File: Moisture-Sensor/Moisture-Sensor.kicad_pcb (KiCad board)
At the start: 2 copper layers, 20 x 100 mm, 18 parts, among them J1 Input, U1 LMV358, U2 NE555

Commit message: half layed out, switch to other computer
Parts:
- D1: value LED -> Green 2.2V 20mA
- J1: footprint Connector_PinSocket_2.54mm:PinSocket_1x03_P2.54mm_Vertical -> Connector_PinHeader_2.54mm:PinHeader_1x03_P2.54mm_Vertical
- R1: value R -> 150 ohm
- moved R7 33.8 mm to (138.4, 71.6)
- moved R4 31.4 mm to (135.6, 61.0), turned to 0 degrees
- moved R5 29.5 mm to (135.6, 62.7), turned to 180 degrees
- moved D1 27.8 mm to (116.3, 52.2), turned to 0 degrees
- moved C1 26.0 mm to (135.9, 67.1)
- moved R3 18.3 mm to (104.9, 58.4), turned to 0 degrees
- moved R6 17.0 mm to (109.2, 57.9), turned to 180 degrees
- moved R1 15.0 mm to (116.2, 54.3), turned to 0 degrees
- moved C5 14.4 mm to (109.2, 56.4), turned to 180 degrees
- moved R2 14.4 mm to (104.9, 56.9), turned to 0 degrees
- moved U1 10.2 mm to (103.9, 63.0)
- moved U2 9.41 mm to (115.8, 63.3)
- moved C4 7.17 mm to (112.3, 65.5)
- moved D2 6.59 mm to (114.3, 73.4), turned to 180 degrees
- moved C3 4.97 mm to (104.9, 67.6), turned to 0 degrees
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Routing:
- net +5V: track 0.00 -> 7.20 mm
- net Net-(D1-Pad2): track 0.00 -> 2.12 mm
- added copper zone on B.Cu, net GND
- added copper zone on F.Cu, net GND
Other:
- net class Default: clearance 0.2 -> 0.254; trace_width 0.25 -> 0.254
- rule trace_clearance: 0.2 -> 0.254
- board text added: "Max Depth"
- board text added: "V1.0"
- board text added: "s + -"

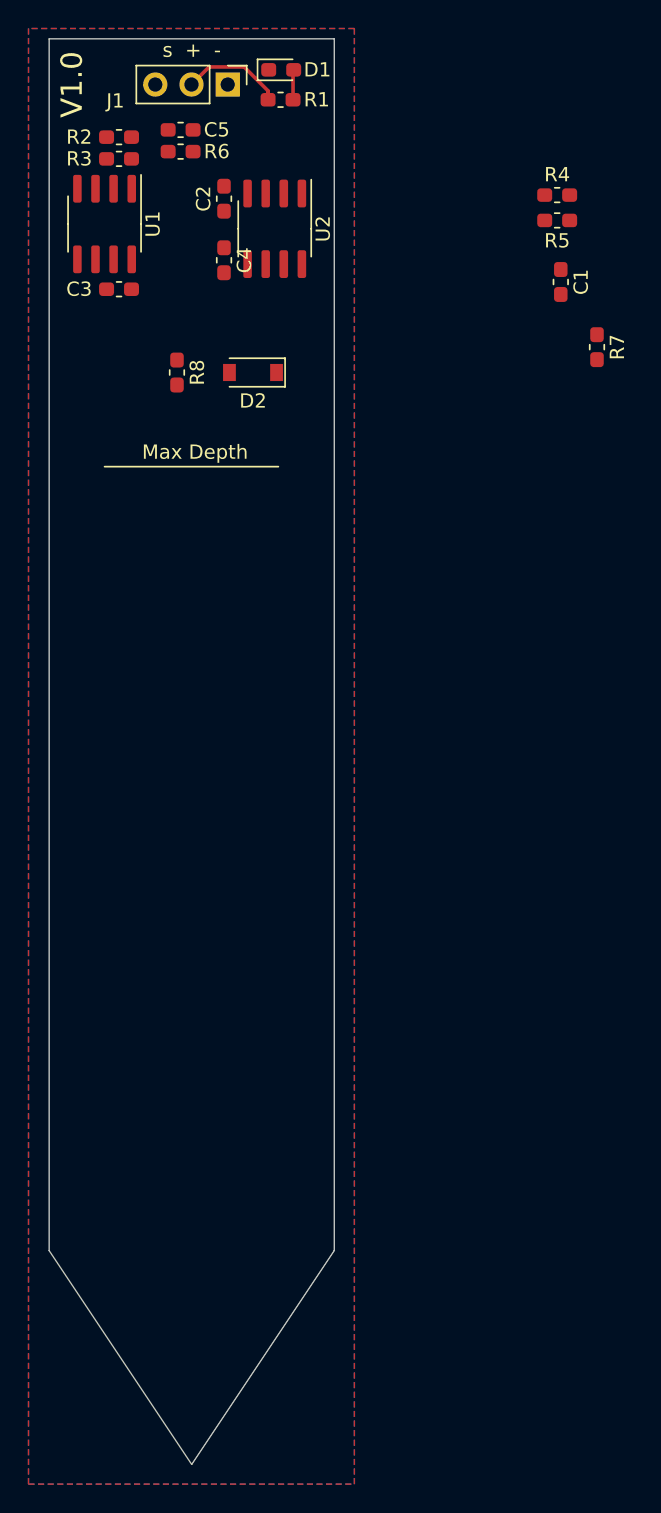
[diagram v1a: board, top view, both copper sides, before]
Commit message: Almost done routing, need to move bypass caps
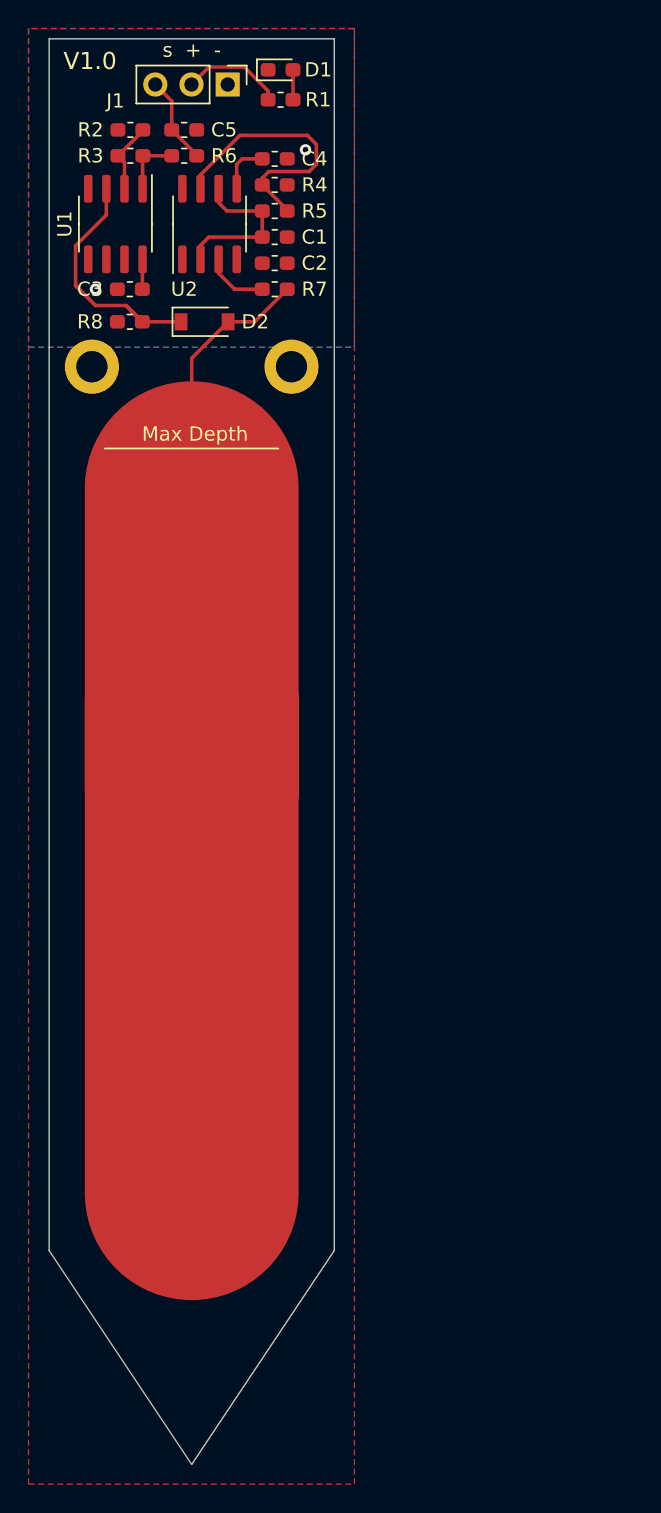
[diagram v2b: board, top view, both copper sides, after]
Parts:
- added H1: M2, MountingHole:MountingHole_2.2mm_M2_ISO14580_Pad, F.Cu at (103.0, 73.0)
- added H2: M2, MountingHole:MountingHole_2.2mm_M2_ISO14580_Pad, F.Cu at (117.0, 73.0)
- moved R7 23.0 mm to (115.8, 67.6), turned to 0 degrees
- moved C1 20.3 mm to (115.8, 63.9), turned to 180 degrees
- moved R4 19.8 mm to (115.8, 60.2), turned to 180 degrees
- moved R5 19.8 mm to (115.8, 62.1)
- moved C4 7.95 mm to (115.8, 58.4), turned to 180 degrees
- moved C2 5.75 mm to (115.8, 65.7), turned to 180 degrees
- moved D2 4.92 mm to (110.9, 69.8), turned to 0 degrees
- moved R8 4.85 mm to (105.7, 69.8), turned to 180 degrees
- moved U2 4.58 mm to (111.3, 63.0), turned to 90 degrees
- moved R2 0.94 mm to (105.7, 56.4)
- moved R3 0.82 mm to (105.7, 58.2)
- moved C3 0.76 mm to (105.7, 67.6)
- moved U1 0.76 mm to (104.6, 63.0)
- moved R6 0.39 mm to (109.5, 58.2), turned to 0 degrees
- moved C5 0.25 mm to (109.5, 56.4)
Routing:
- net Net-(D2-Pad2): track 0.00 -> 72.3 mm
- net Net-(D2-Pad1): track 0.00 -> 19.1 mm
- net Net-(R4-Pad2): track 0.00 -> 19.1 mm
- net Net-(C1-Pad2): track 0.00 -> 11.7 mm
- net Sig: track 0.00 -> 6.20 mm
- net Net-(R2-Pad2): track 0.00 -> 5.04 mm
- net Net-(R7-Pad1): track 0.00 -> 4.50 mm
- net Net-(R3-Pad2): track 0.00 -> 4.35 mm
- net Net-(C4-Pad2): track 0.00 -> 3.67 mm
- net +5V: track 7.20 -> 9.30 mm
- net GND: vias 0 -> 2

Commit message: Layout looks good and passed DRC
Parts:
- moved C4 11.0 mm to (109.7, 67.6)
- moved R7 9.16 mm to (115.3, 58.4)
- moved C1 0.50 mm to (115.3, 63.9)
- moved C2 0.50 mm to (115.3, 65.7)
- moved C3 0.50 mm to (105.2, 67.6)
- moved C5 0.50 mm to (109.0, 56.4)
- moved D2 0.50 mm to (110.4, 69.8)
- moved R2 0.50 mm to (105.2, 56.4)
- moved R3 0.50 mm to (105.2, 58.2)
- moved R4 0.50 mm to (115.3, 60.2)
- moved R5 0.50 mm to (115.3, 62.1)
- moved R6 0.50 mm to (109.0, 58.2)
- moved R8 0.50 mm to (105.2, 69.8)
- moved U1 0.50 mm to (104.1, 63.0)
- moved U2 0.50 mm to (110.8, 63.0), turned to 270 degrees
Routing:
- net +5V: track 9.30 -> 53.6 mm, vias 0 -> 2
- net Net-(D2-Pad2): track 72.3 -> 81.2 mm
- net Net-(R7-Pad1): track 4.50 -> 8.14 mm
- net Net-(R4-Pad2): track 19.1 -> 17.5 mm
- net Net-(C4-Pad2): track 3.67 -> 2.11 mm
- net GND: vias 2 -> 4
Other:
- net class Default: clearance 0.254 -> 0.2032
- rule trace_clearance: 0.254 -> 0.2032
